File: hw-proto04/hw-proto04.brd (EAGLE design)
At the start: 54.3 x 62.2 mm, 27 parts, among them IC2 UCC27523DR, IC3 MCP2562T, J1 10, J2 10, Q1 SQJ147ELP-T1_GE3, Q2 SQJ147ELP-T1_GE3

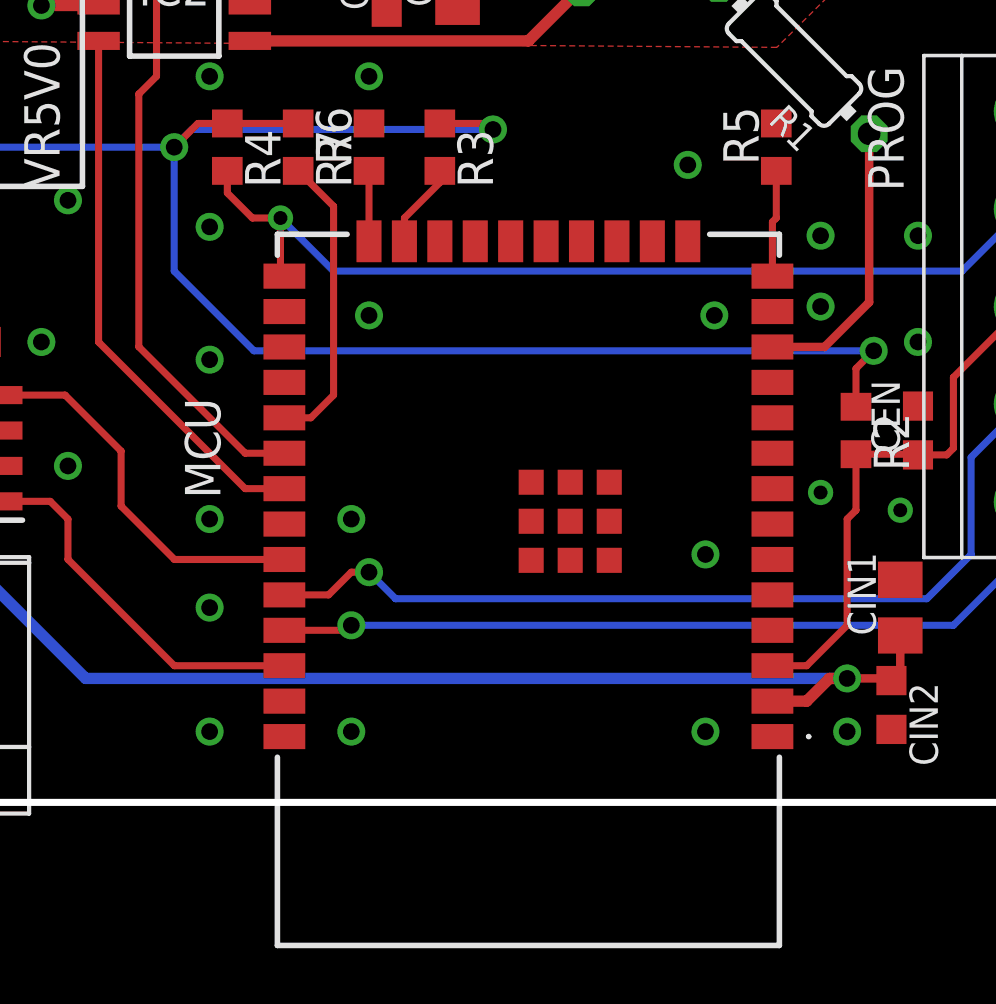
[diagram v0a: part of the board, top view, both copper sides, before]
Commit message: swap esp32 for stm32
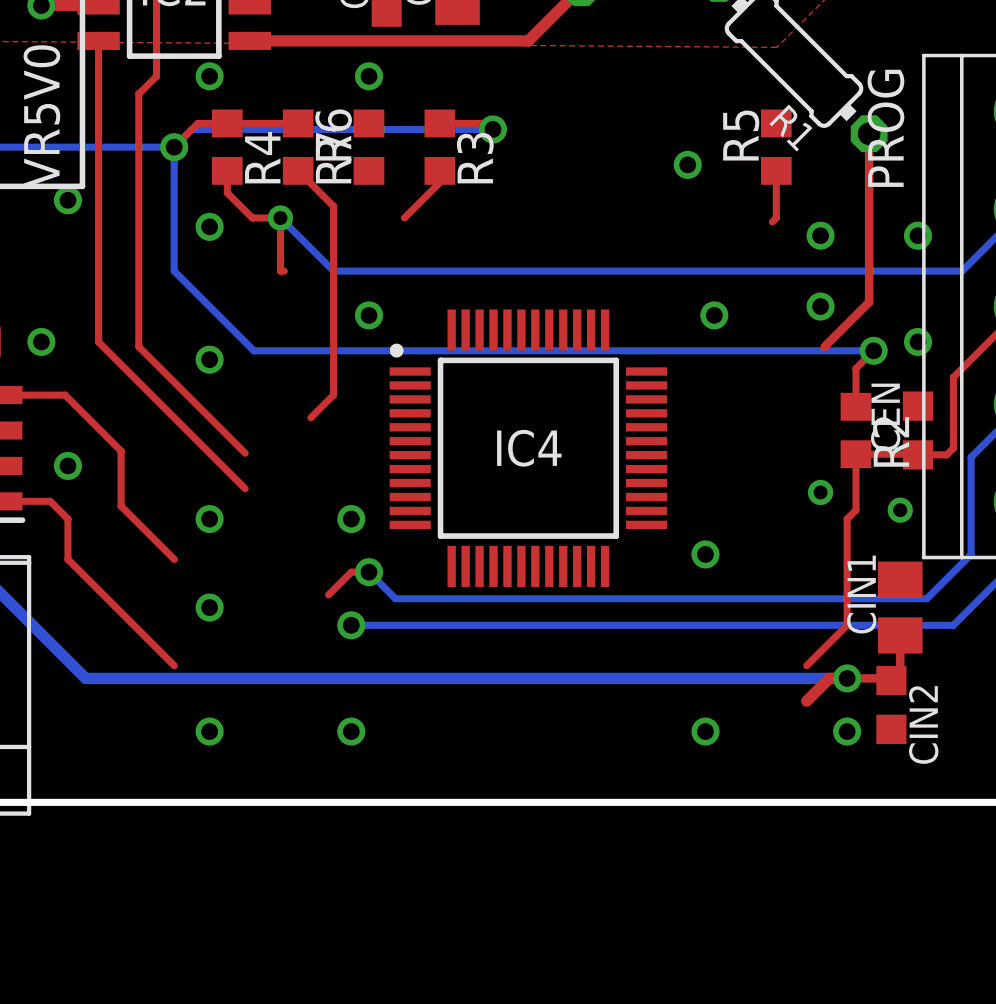
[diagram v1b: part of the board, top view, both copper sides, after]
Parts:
- removed MCU: ESP32-WROOM-32E, ESP32-WROOM-32E-N8R2:ESP32WROOM32EN8R2
- added IC4: STM32F042C6T7, STM32F042C6T7:QFP50P900X900X160-48N
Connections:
- removed net CTL4: MCU.11
- net +3V3: now also IC4.24, IC4.36, IC4.48; no longer MCU.2
- net CAN_RX: no longer MCU.33
- net CAN_TX: no longer MCU.36
- net CTL1: no longer MCU.30
- net CTL2: no longer MCU.31
- net CTL3: no longer MCU.12
- net EN: no longer MCU.3
- net GND: now also IC4.23, IC4.47; no longer MCU.1, MCU.15, MCU.38, MCU.39, MCU.40, MCU.41, MCU.42, MCU.43, MCU.44, MCU.45, MCU.46, MCU.47
- net GPIO0: no longer MCU.25
- net GPIO12: no longer MCU.14
- net GPIO15: no longer MCU.23
- net GPIO2: no longer MCU.24
- net GPIO5: no longer MCU.29
- net RXD0: no longer MCU.34
- net TXD0: no longer MCU.35
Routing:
- net CAN_TX: track 13.4 -> 9.48 mm
- net CAN_RX: track 13.7 -> 9.80 mm
- net GPIO2: track 2.52 -> 0.00 mm
- net TXD0: track 29.5 -> 27.3 mm
- net GPIO12: track 3.83 -> 1.89 mm
- net CTL3: track 10.2 -> 8.31 mm
- net RXD0: track 32.2 -> 30.6 mm
- net CTL2: track 19.6 -> 18.2 mm
- net CTL1: track 22.3 -> 20.9 mm
- net EN: track 19.3 -> 18.1 mm
- net +3V3: track 140.9 -> 139.7 mm
- net GPIO5: track 10.7 -> 9.72 mm
- net GPIO15: track 3.05 -> 2.22 mm
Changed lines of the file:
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@@
 <attribute name="VALUE" x="28.258" y="54.864" size="1.27" layer="27" align="center"/>
-</element>
-<element name="MCU" library="ESP32-WROOM-32E-N8R2" package="ESP32WROOM32EN8R2" value="ESP32-WROOM-32E" x="35.56" y="8.89" smashed="yes" rot="R180">
-<attribute name="MANUFACTURER_PART_NUMBER" value="ESP32-WROOM-32E-N8R2" x="35.56" y="8.89" size="1.778" layer="27" rot="R180" display="off"/>
-<attribute name="DESCRIPTION" value="Multiprotocol Modules ESP32-WROOM-32E integrates ESP32-D0WD-V3, with higher stability and safety performance." x="35.56" y="8.89" size="1.778" layer="27" rot="R180" display="off"/>
-<attribute name="MANUFACTURER_NAME" value="Espressif Systems" x="35.56" y="8.89" size="1.778" layer="27" rot="R180" display="off"/>
-<attribute name="MOUSER_PART_NUMBER" value="356-ESP32WRM32EN8R2" x="35.56" y="8.89" size="1.778" layer="27" rot="R180" display="off"/>
-<attribute name="HEIGHT" value="3.25mm" x="35.56" y="8.89" size="1.778" layer="27" rot="R180" display="off"/>
-<attribute name="MOUSER_PRICE-STOCK" value="https://www.mouser.co.uk/ProductDetail/Espressif-Systems/ESP32-WROOM-32E-N8R2?qs=By6Nw2ByBD0mvGJSS3Ohlw%3D%3D" x="35.56" y="8.89" size="1.778" layer="27" rot="R180" display="off"/>
-<attribute name="NAME" x="23.88" y="13.97" size="1.27" layer="25" rot="R270" align="center"/>
-<attribute name="VALUE" x="35.56" y="4.06" size="1.27" layer="27" rot="R180" align="center"/>
 </element>
 <element name="VR3V3" library="TSR_1-2433E" package="TSR-1-2433" value="+3V3" x="5.08" y="29.21" smashed="yes" rot="R270">
@@
 <element name="CDRV2" library="rcl" package="C0805K" value="4u7" x="33.02" y="30.7975" rot="R90"/>
 <element name="CDRV1" library="rcl" package="C0603K" value="100n" x="30.48" y="30.48" rot="R90"/>
+<element name="IC4" library="STM32F042C6T7" package="QFP50P900X900X160-48N" value="STM32F042C6T7" x="35.56" y="13.97">
+<attribute name="MOUSER_PRICE-STOCK" value="https://www.mouser.co.uk/ProductDetail/STMicroelectronics/STM32F042C6T7?qs=PqoDHHvF6499eidad5TESA%3D%3D" x="35.56" y="13.97" size="1.778" layer="27" display="off"/>
+<attribute name="DESCRIPTION" value="Mainstream Arm Cortex-M0 USB line MCU with 32 Kbytes of Flash memory, 48 MHz CPU, USB, CAN and CEC functions" x="35.56" y="13.97" size="1.778" layer="27" display="off"/>
+<attribute name="MANUFACTURER_NAME" value="STMicroelectronics" x="35.56" y="13.97" size="1.778" layer="27" display="off"/>
+<attribute name="MANUFACTURER_PART_NUMBER" value="STM32F042C6T7" x="35.56" y="13.97" size="1.778" layer="27" display="off"/>
+<attribute name="HEIGHT" value="1.6mm" x="35.56" y="13.97" size="1.778" layer="27" display="off"/>
+<attribute name="MOUSER_PART_NUMBER" value="511-STM32F042C6T7" x="35.56" y="13.97" size="1.778" layer="27" display="off"/>
+</element>
 </elements>
 <signals>
@@
 </signal>
 <signal name="GND">
-<contactref element="MCU" pad="38"/>
-<contactref element="MCU" pad="47"/>
-<contactref element="MCU" pad="46"/>
-<contactref element="MCU" pad="45"/>
-<contactref element="MCU" pad="44"/>
-<contactref element="MCU" pad="43"/>
-<contactref element="MCU" pad="42"/>
-<contactref element="MCU" pad="41"/>
-<contactref element="MCU" pad="40"/>
-<contactref element="MCU" pad="39"/>
-<contactref element="MCU" pad="1"/>
-<contactref element="MCU" pad="15"/>
 <contactref element="IC1" pad="1"/>
 <contactref element="VR3V3" pad="2"/>
@@
 <via x="8.89" y="12.7" extent="1-16" drill="0.6"/>
 <contactref element="CAN" pad="2"/>
+<contactref element="IC4" pad="23"/>
+<contactref element="IC4" pad="47"/>
+<wire x1="29.845" y1="18.7325" x2="33.31" y2="18.208" width="0" layer="19" extent="1-1"/>
+<wire x1="37.81" y1="9.732" x2="41.91" y2="10.16" width="0" layer="19" extent="1-1"/>
 </signal>
 <signal name="SW1">
@@
 <signal name="+3V3">
 <contactref element="VR3V3" pad="3"/>
-<contactref element="MCU" pad="2"/>
 <contactref element="IC3" pad="5"/>
-<wire x1="44.31" y1="4.9" x2="45.54" y2="4.9" width="0.4064" layer="1"/>
 <wire x1="45.54" y1="4.9" x2="46.355" y2="5.715" width="0.4064" layer="1"/>
 <wire x1="46.355" y1="5.715" x2="46.99" y2="5.715" width="0.4064" layer="1"/>
@@
 <wire x1="47.3075" y1="15.455" x2="47.3075" y2="16.8275" width="0.254" layer="1"/>
 <wire x1="47.3075" y1="16.8275" x2="47.9425" y2="17.4625" width="0.254" layer="1"/>
+<contactref element="IC4" pad="24"/>
+<contactref element="IC4" pad="36"/>
+<contactref element="IC4" pad="48"/>
+<wire x1="32.81" y1="18.208" x2="39.798" y2="16.72" width="0" layer="19" extent="1-1"/>
+<wire x1="25.7175" y1="17.4625" x2="32.81" y2="18.208" width="0" layer="19" extent="1-16"/>
+<wire x1="38.31" y1="9.732" x2="39.798" y2="16.72" width="0" layer="19" extent="1-1"/>
 </signal>
 <signal name="+12V">
@@
 <wire x1="14.365" y1="26.275" x2="14.365" y2="17.78" width="0.3048" layer="1"/>
 </signal>
-<signal name="CTL4">
-<contactref element="MCU" pad="11"/>
-</signal>
 <signal name="CTL3">
 <contactref element="R1" pad="1"/>
-<contactref element="MCU" pad="12"/>
-<wire x1="44.31" y1="17.6" x2="46.175" y2="17.6" width="0.3048" layer="1"/>
 <wire x1="46.175" y1="17.6" x2="47.779075" y2="19.204075" width="0.3048" layer="1"/>
 <wire x1="47.779075" y1="25.245921875" x2="47.779075" y2="19.204075" width="0.3048" layer="1"/>
@@
 </signal>
 <signal name="CTL2">
-<wire x1="26.81" y1="12.52" x2="25.404246875" y2="12.52" width="0.254" layer="1"/>
 <wire x1="25.404246875" y1="12.52" x2="20.148" y2="17.776246875" width="0.254" layer="1"/>
-<contactref element="MCU" pad="31"/>
 <contactref element="IC2" pad="4"/>
 <wire x1="20.148" y1="28.575" x2="20.148" y2="17.776246875" width="0.254" layer="1"/>
 </signal>
 <signal name="CTL1">
-<wire x1="26.81" y1="13.79" x2="25.40636875" y2="13.79" width="0.254" layer="1"/>
 <wire x1="25.40636875" y1="13.79" x2="21.59" y2="17.60636875" width="0.254" layer="1"/>
-<contactref element="MCU" pad="30"/>
 <wire x1="21.59" y1="17.60636875" x2="21.59" y2="26.67" width="0.254" layer="1"/>
 <wire x1="21.59" y1="26.67" x2="22.225" y2="27.305" width="0.254" layer="1"/>
@@
 <signal name="CAN_TX">
 <contactref element="IC3" pad="1"/>
-<contactref element="MCU" pad="36"/>
 <wire x1="16.67" y1="12.065" x2="18.415" y2="12.065" width="0.254" layer="1"/>
 <wire x1="18.415" y1="12.065" x2="19.05" y2="11.43" width="0.254" layer="1"/>
-<wire x1="26.81" y1="6.17" x2="22.864246875" y2="6.17" width="0.254" layer="1"/>
 <wire x1="22.864246875" y1="6.17" x2="19.05" y2="9.984246875" width="0.254" layer="1"/>
 <wire x1="19.05" y1="9.984246875" x2="19.05" y2="11.43" width="0.254" layer="1"/>
@@
 <signal name="CAN_RX">
 <contactref element="IC3" pad="4"/>
-<contactref element="MCU" pad="33"/>
 <wire x1="20.955" y1="13.86695625" x2="20.955" y2="11.893484375" width="0.254" layer="1"/>
 <wire x1="20.955" y1="11.893484375" x2="22.868484375" y2="9.98" width="0.254" layer="1"/>
-<wire x1="22.868484375" y1="9.98" x2="26.81" y2="9.98" width="0.254" layer="1"/>
 <wire x1="16.67" y1="15.875" x2="18.94695625" y2="15.875" width="0.254" layer="1"/>
 <wire x1="18.94695625" y1="15.875" x2="20.955" y2="13.86695625" width="0.254" layer="1"/>
@@
 </signal>
 <signal name="GPIO15">
-<contactref element="MCU" pad="23"/>
 <contactref element="R3" pad="2"/>
-<wire x1="31.115" y1="21.39" x2="31.115" y2="22.225" width="0.254" layer="1"/>
 <wire x1="31.115" y1="22.225" x2="32.385" y2="23.495" width="0.254" layer="1"/>
 <wire x1="32.385" y1="23.495" x2="32.385" y2="23.915" width="0.254" layer="1"/>
@@
 <signal name="GPIO12">
 <contactref element="R5" pad="1"/>
-<contactref element="MCU" pad="14"/>
-<wire x1="44.31" y1="20.14" x2="44.31" y2="22.085" width="0.254" layer="1"/>
 <wire x1="44.31" y1="22.085" x2="44.45" y2="22.225" width="0.254" layer="1"/>
 <wire x1="44.45" y1="22.225" x2="44.45" y2="23.915" width="0.254" layer="1"/>
@@
 <signal name="GPIO2">
 <contactref element="R6" pad="1"/>
-<contactref element="MCU" pad="24"/>
-<wire x1="29.845" y1="21.39" x2="29.845" y2="23.915" width="0.254" layer="1"/>
 </signal>
 <signal name="GPIO0">
-<contactref element="MCU" pad="25"/>
 <contactref element="R4" pad="2"/>
 <contactref element="PROG" pad="4"/>
 <wire x1="51.11" y1="20.32" x2="28.575" y2="20.32" width="0.254" layer="16"/>
-<wire x1="26.81" y1="20.32" x2="26.81" y2="20.14" width="0.254" layer="1"/>
 <wire x1="51.11" y1="20.32" x2="53.34" y2="22.55" width="0.254" layer="16"/>
 <wire x1="26.67" y1="22.225" x2="25.663025" y2="22.225" width="0.254" layer="1"/>
@@
 <signal name="GPIO5">
 <contactref element="R7" pad="2"/>
-<contactref element="MCU" pad="29"/>
 <wire x1="27.305" y1="23.915" x2="28.575" y2="22.645" width="0.254" layer="1"/>
 <wire x1="28.575" y1="22.645" x2="28.575" y2="15.875" width="0.254" layer="1"/>
-<wire x1="26.81" y1="15.06" x2="27.76" y2="15.06" width="0.254" layer="1"/>
 <wire x1="27.76" y1="15.06" x2="28.575" y2="15.875" width="0.254" layer="1"/>
 </signal>
 <signal name="EN">
-<contactref element="MCU" pad="3"/>
 <contactref element="PROG" pad="3"/>
-<wire x1="44.31" y1="6.17" x2="45.54" y2="6.17" width="0.254" layer="1"/>
 <wire x1="45.54" y1="6.17" x2="46.99" y2="7.62" width="0.254" layer="1"/>
 <contactref element="R2" pad="2"/>
@@
 </signal>
 <signal name="RXD0">
-<contactref element="MCU" pad="34"/>
 <contactref element="PROG" pad="2"/>
 <via x="29.845" y="9.525" extent="1-16" drill="0.6"/>
-<wire x1="26.81" y1="8.71" x2="28.395" y2="8.71" width="0.254" layer="1"/>
 <wire x1="28.395" y1="8.71" x2="29.21" y2="9.525" width="0.254" layer="1"/>
 <wire x1="29.21" y1="9.525" x2="29.845" y2="9.525" width="0.254" layer="1"/>
@@
 </signal>
 <signal name="TXD0">
-<contactref element="MCU" pad="35"/>
 <contactref element="PROG" pad="1"/>
 <wire x1="53.34" y1="10.16" x2="53.34" y2="12.05" width="0.254" layer="16"/>
-<wire x1="26.81" y1="7.44" x2="29.03" y2="7.44" width="0.254" layer="1"/>
 <wire x1="29.03" y1="7.44" x2="29.21" y2="7.62" width="0.254" layer="1"/>
 <via x="29.21" y="7.62" extent="1-16" drill="0.6"/>

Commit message: work on new layout
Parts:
- removed VR3V3: +3V3, TSR_1-2433E:TSR-1-2433
- added C3, C4, C5, C6: 1u, rcl:C0603K
- added IC5: TLV74333PDBVR, TLV74333PDBVR:SOT95P280X145-5N
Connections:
- net +12V: now also C5.1; no longer VR3V3.1
- net +3V3: now also C4.1, IC5.5; no longer VR3V3.3
- net +5V: now also C3.1, C6.1, IC5.1, IC5.3
- net GND: now also C3.2, C4.2, C5.2, C6.2, IC5.2; no longer VR3V3.2
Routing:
- net +3V3: track 139.7 -> 131.4 mm
- net +12V: track 9.94 -> 6.13 mm

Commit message: schematic updates
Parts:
- removed CIN1: 22u, rcl:C0805K
- added CVDD, CVDDIO2: 4u7, rcl:C0603K
- added CVDD1, CVDDIO: 100n, rcl:C0603K
- added CVDDA1: 10n, rcl:C0603K
- added CVDDA2: 1u, rcl:C0603K
- CNRST: value 1u -> 100n
- renumbered CEN to CNRST, CIN2 to VDD2
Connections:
- new net N$8: CNRST.1, IC4.7
- net +3V3: now also CVDD.1, CVDD1.1, CVDDA1.1, CVDDA2.1, CVDDIO.1, CVDDIO2.1, IC4.9; no longer CIN1.1
- net EN: no longer CNRST.1
- net GND: now also CVDD.2, CVDD1.2, CVDDA1.2, CVDDA2.2, CVDDIO.2, CVDDIO2.2, IC4.35, IC4.8; no longer CIN1.2
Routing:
- net +3V3: track 131.4 -> 130.1 mm
- net EN: track 18.1 -> 17.0 mm

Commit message: schematic updates
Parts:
- removed R2: 10K0, rcl:R0603
- removed R3, R4, R5, R6, R7: 47K0, rcl:R0603
- renumbered CVDDA1 to CVDA1, CVDDA2 to CVDA2, VDD2 to CVDD2
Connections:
- removed net GPIO12: R5.1
- removed net GPIO15: R3.2
- removed net GPIO2: R6.1
- removed net GPIO5: R7.2
- new net CAN_RX_ALT: IC4.45
- new net CAN_TX_ALT: IC4.46
- new net RX: IC4.31
- new net TX: IC4.30
- net +3V3: no longer R2.1, R3.1, R4.1, R7.1
- net CAN_RX: now also IC4.32
- net CAN_TX: now also IC4.33
- net EN: no longer R2.2
- net GND: no longer R5.2, R6.2
- net GPIO0: no longer R4.2
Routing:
- net EN: track 17.0 -> 6.47 mm
- net GPIO5: track 9.72 -> 0.00 mm
- net +3V3: track 130.1 -> 121.7 mm, vias 5 -> 4
- net GPIO15: track 2.22 -> 0.00 mm
- net GPIO12: track 1.89 -> 0.00 mm
- net GPIO0: track 33.5 -> 32.7 mm
- net GND: vias 45 -> 25

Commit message: layout, routing and schematic refinement
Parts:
- removed C1, C2: 100n, rcl:C0603K
- removed C3, C4, C5, C6: 1u, rcl:C0603K
- removed PROG: 1X5, adafruit:1X05-3.5MM
- added C3V1, C3V2, C5V1, C5V2: 1u, rcl:C0603K
- added CCAN1, CCAN2: 100n, rcl:C0603K
- added PRG, SER: (no value), SparkFun-Connectors:1X04_LOCK
- moved CVDDIO 75.2 mm to (24.4, 20.3)
- moved CVDD 64.1 mm to (16.5, 21.3), turned to 90 degrees
- moved CVDDIO2 59.5 mm to (24.4, 18.7)
- moved CVDA2 57.3 mm to (11.4, 10.5), turned to 180 degrees
- moved CVDD1 49.0 mm to (14.9, 21.3), turned to 90 degrees
- moved CVDA1 44.1 mm to (11.4, 12.1), turned to 180 degrees
- moved CNRST 38.1 mm to (11.4, 13.7), turned to 180 degrees
- moved CAN 34.3 mm to (44.5, 7.62)
- moved IC3 32.0 mm to (45.7, 17.8), turned to 0 degrees
- moved CVDD2 24.6 mm to (24.4, 9.53), turned to 0 degrees
- moved IC4 16.5 mm to (19.1, 14.0)
- moved IC5 11.5 mm to (6.35, 10.2)
- moved VR5V0 7.18 mm to (8.89, 24.1), turned to 0 degrees
- moved CDRV1 5.08 mm to (30.5, 25.4)
- moved IC2 5.08 mm to (22.9, 25.4)
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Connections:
- removed net EN: PROG.3
- removed net GPIO0: PROG.4
- removed net RX: IC4.31
- removed net RXD0: PROG.2
- removed net TX: IC4.30
- removed net TXD0: PROG.1
- new net RX1: IC4.31, SER.3
- new net SWCLK: IC4.20, PRG.3
- new net SWDIO: IC4.19, PRG.2
- new net TX1: IC4.30, SER.2
- net +12V: now also C5V1.1; no longer C5.1
- net +3V3: now also C3V2.1, CCAN2.1, PRG.1, SER.4; no longer C2.1, C4.1
- net +5V: now also C3V1.1, C5V2.1, CCAN1.1; no longer C1.1, C3.1, C6.1
- net CTL1: now also IC4.39
- net CTL2: now also IC4.40
- net CTL3: now also IC4.34
- net GND: now also C3V1.2, C3V2.2, C5V1.2, C5V2.2, CCAN1.2, CCAN2.2, PRG.4, SER.1; no longer C1.2, C2.2, C3.2, C4.2, C5.2, C6.2, PROG.5
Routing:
- net +3V3: track 121.7 -> 79.0 mm, vias 4 -> 2
- net +5V: track 14.5 -> 56.3 mm, vias 0 -> 2
- net GPIO0: track 32.7 -> 0.00 mm, vias 1 -> 0
- net RXD0: track 30.6 -> 0.00 mm, vias 1 -> 0
- net TXD0: track 27.3 -> 0.00 mm, vias 1 -> 0
- net CTL1: track 20.9 -> 0.00 mm
- net CTL2: track 18.2 -> 0.00 mm
- net RX1: track 0.00 -> 14.9 mm
- net TX1: track 0.00 -> 12.4 mm
- net CTL3: track 8.31 -> 20.4 mm
- net CAN_TX: track 9.48 -> 21.6 mm
- net CAN_RX: track 9.80 -> 20.2 mm
- net EN: track 6.47 -> 0.00 mm
- net SWDIO: track 0.00 -> 6.44 mm
- net N$1: track 11.1 -> 16.5 mm
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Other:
- board size 54.3 x 62.2 mm -> 54.3 x 58.4 mm
